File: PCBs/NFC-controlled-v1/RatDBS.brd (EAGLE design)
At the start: 25.4 x 15.9 mm, 20 parts

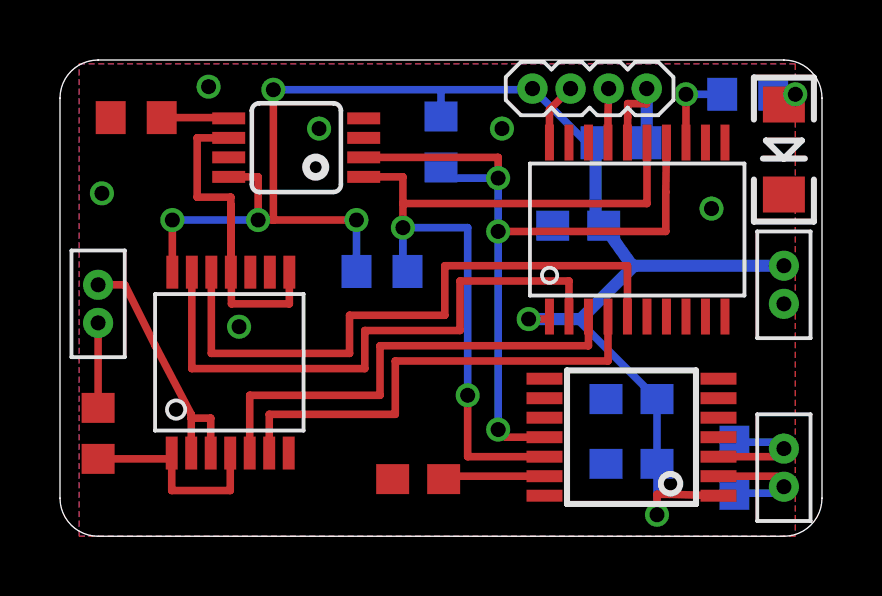
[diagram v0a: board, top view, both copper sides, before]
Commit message: Found bug in PCB - switch matrix not wired up correctly. Fixed, and added interrupt and reset connections to MSP430
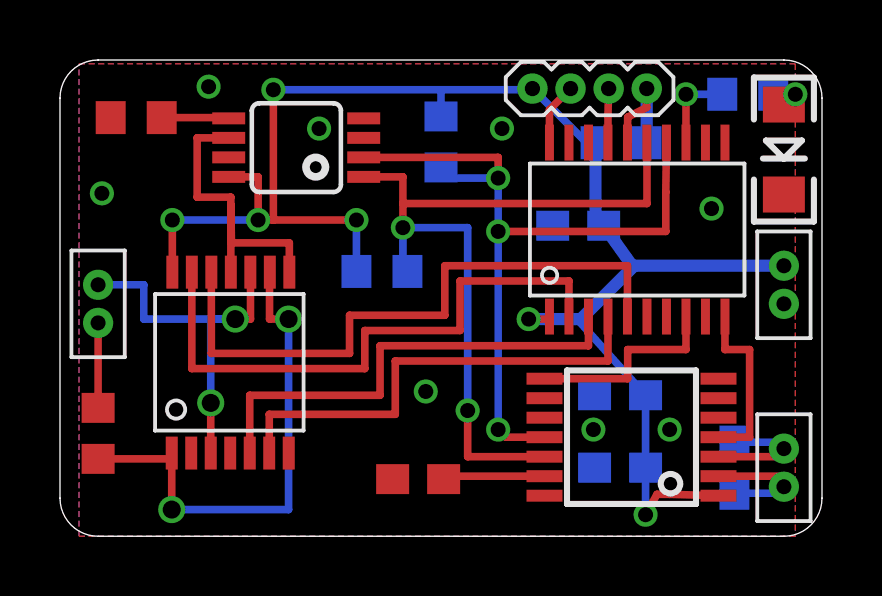
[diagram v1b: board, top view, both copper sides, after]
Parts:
- moved C1 0.40 mm to (18.7, 4.70)
- moved C2 0.40 mm to (18.7, 2.29)
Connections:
- new net N$3: MSP430.8, U$1.8
- new net N$7: MSP430.10, U$1.4
- net GND: now also TS3A4751_0.2, TS3A4751_0.4; no longer TS3A4751_0.10, TS3A4751_0.9
- net STIM_OUT1: now also TS3A4751_0.9; no longer TS3A4751_0.4
- net STIM_OUT2: now also TS3A4751_0.10; no longer TS3A4751_0.2
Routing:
- net STIM_OUT1: track 6.90 -> 16.8 mm, vias 0 -> 2
- net N$3: track 0.00 -> 6.79 mm
- net N$7: track 0.00 -> 5.88 mm
- net STIM_OUT2: track 8.85 -> 13.1 mm, vias 0 -> 2
- net STIM_IN: track 12.9 -> 10.8 mm
- net GND: vias 6 -> 8
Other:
- board text added: "NFC-RDBS v1.1 Kemere Lab (C)2015"
- board text removed: "NFC-RDBS v1 Kemere Lab (C)2015"
